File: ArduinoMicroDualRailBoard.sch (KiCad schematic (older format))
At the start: 56 parts, among them J1 Conn_01x20_Male, J10 Conn_01x02_Male, J2 Screw_Terminal_01x03, J3 Conn_01x20_Male, J4 Conn_01x20_Male, J5 Screw_Terminal_01x03, J6 Conn_01x20_Male, J7 SDS-50J, J8 SDS-50J, J9 Screw_Terminal_01x03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

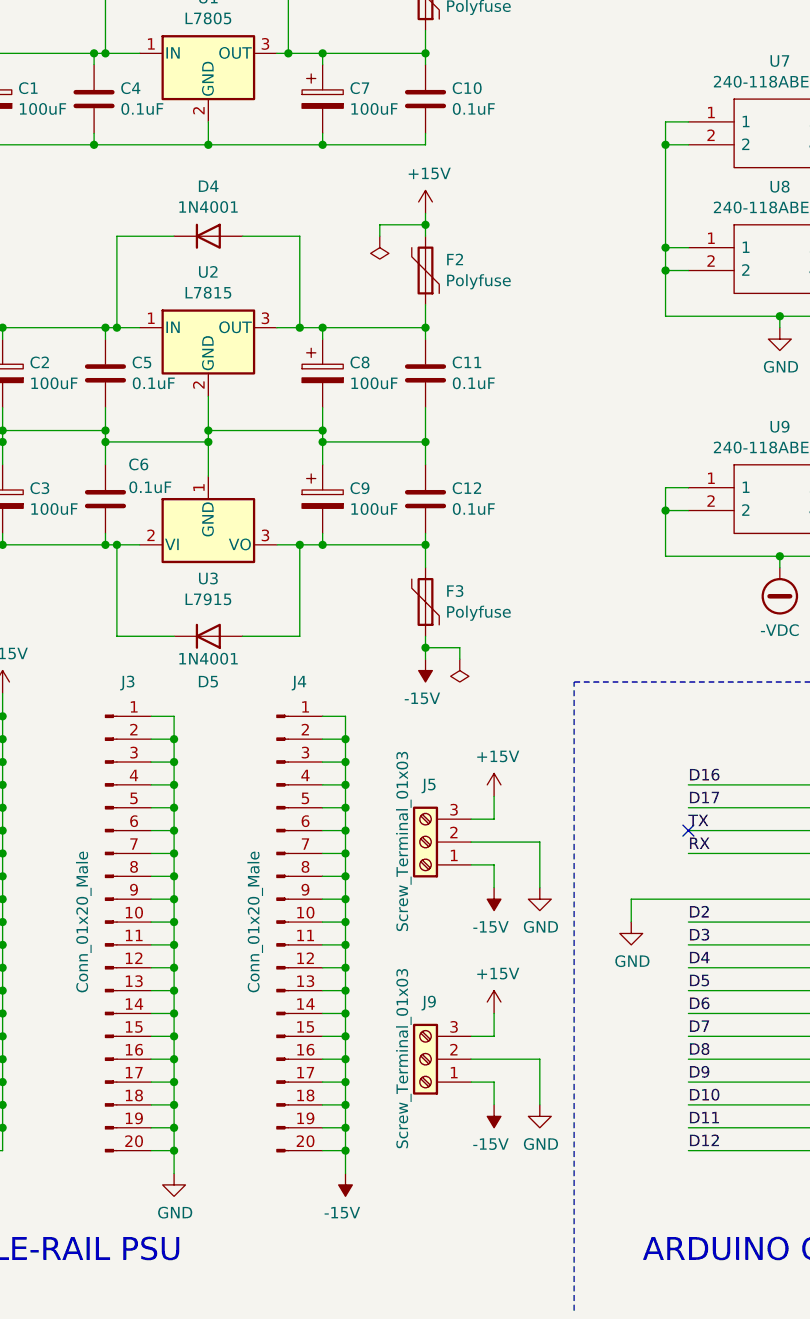
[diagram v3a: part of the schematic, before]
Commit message: Lots of small fixes * Added protection diodes on +/- 15V rails * Fixed 7915 diode direction * Flipped Arduino socket so the USB can actually be plugged in * Added +5V out (since it might be useful to have)
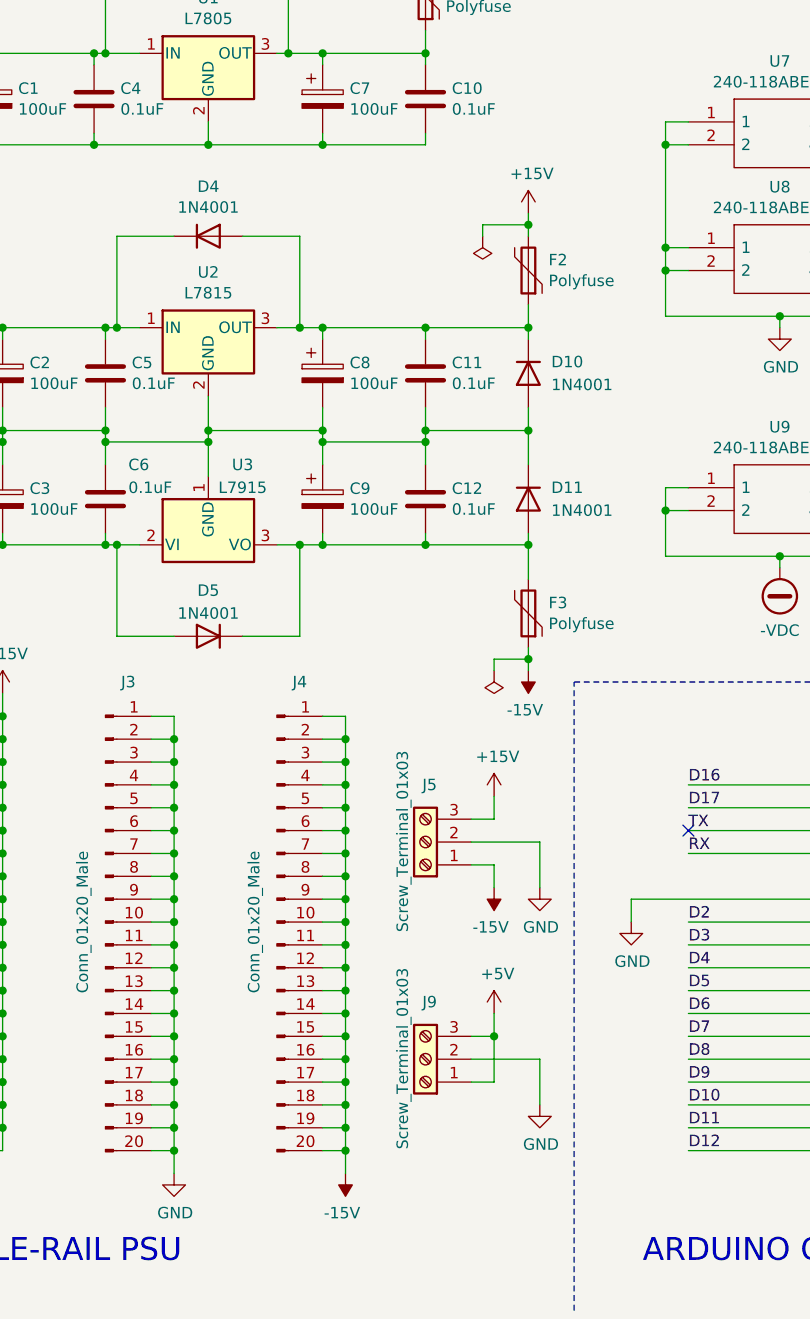
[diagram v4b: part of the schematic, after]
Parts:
- added D10, D11: 1N4001, Diode_THT:D_DO-41_SOD81_P10.16mm_Horizontal, symbol Diode:1N4001
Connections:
- net +15V: no longer J9.3 (Pin_3)
- net +5V: now also J9.1 (Pin_1), J9.3 (Pin_3)
- net -15V: no longer J9.1 (Pin_1)
- net -VDC: now also D5.2 (A); no longer D5.1 (K)
- net GND: now also D10.2 (A), D11.1 (K)
- net at C12.2, C9.2, F3.2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: now also D5.1 (K), D11.2 (A); no longer D5.2 (A)
- net at C11.1, C8.1, D4.2 (A)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: now also D10.1 (K)
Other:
- moved on the sheet: F2, F3
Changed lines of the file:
@@
 L power:+15V #PWR0104
 U 1 1 5FC58BBA
-P 3050 3000
-F 0 "#PWR0104" H 3050 2850 50  0001 C CNN
-F 1 "+15V" H 3065 3173 50  0000 C CNN
-F 2 "" H 3050 3000 50  0001 C CNN
-F 3 "" H 3050 3000 50  0001 C CNN
-	1    3050 3000
+P 3500 3000
+F 0 "#PWR0104" H 3500 2850 50  0001 C CNN
+F 1 "+15V" H 3515 3173 50  0000 C CNN
+F 2 "" H 3500 3000 50  0001 C CNN
+F 3 "" H 3500 3000 50  0001 C CNN
+	1    3500 3000
 	1    0    0    -1
 $EndComp
@@
 	3050 3500 3050 3550
 Wire Wire Line
-	3050 4000 3050 3850
+	3050 4000 3050 3950
 $Comp
 L Connector:Conn_01x20_Male J1
@@
 L power:-15V #PWR0124
 U 1 1 5FC59348
-P 3050 4950
-F 0 "#PWR0124" H 3050 5050 50  0001 C CNN
-F 1 "-15V" H 3065 5123 50  0000 C CNN
-F 2 "" H 3050 4950 50  0001 C CNN
-F 3 "" H 3050 4950 50  0001 C CNN
-	1    3050 4950
+P 3500 5000
+F 0 "#PWR0124" H 3500 5100 50  0001 C CNN
+F 1 "-15V" H 3515 5173 50  0000 C CNN
+F 2 "" H 3500 5000 50  0001 C CNN
+F 3 "" H 3500 5000 50  0001 C CNN
+	1    3500 5000
 	-1   0    0    1
 $EndComp
@@
 F 3 "http://www.vishay.com/docs/88503/1n4001.pdf" H 2100 4850 50  0001 C CNN
 	1    2100 4850
-	1    0    0    1
+	-1   0    0    -1
 $EndComp
 $Comp
@@
 U 1 1 5FBD82BC
 P 2100 4450
-F 0 "U3" H 2100 4301 50  0000 C CNN
-F 1 "L7915" H 2100 4210 50  0000 C CNN
+F 0 "U3" H 2250 4800 50  0000 C CNN
+F 1 "L7915" H 2250 4700 50  0000 C CNN
 F 2 "Package_TO_SOT_THT:TO-220-3_Vertical" H 2100 4250 50  0001 C CIN
 F 3 "http://www.st.com/content/ccc/resource/technical/document/datasheet/c9/16/86/41/c7/2b/45/f2/CD00000450.pdf/files/CD00000450.pdf/jcr:content/translations/en.CD00000450.pdf" H 2100 4450 50  0001 C CNN
@@
 L Device:Polyfuse F3
 U 1 1 5FC1DF2E
-P 3050 4700
-F 0 "F3" H 2962 4654 50  0000 R CNN
-F 1 "Polyfuse" H 2962 4745 50  0000 R CNN
-F 2 "Capacitor_THT:C_Disc_D8.0mm_W2.5mm_P5.00mm" H 3100 4500 50  0001 L CNN
-F 3 "~" H 3050 4700 50  0001 C CNN
-	1    3050 4700
+P 3500 4750
+F 0 "F3" H 3412 4704 50  0000 R CNN
+F 1 "Polyfuse" H 3412 4795 50  0000 R CNN
+F 2 "Capacitor_THT:C_Disc_D8.0mm_W2.5mm_P5.00mm" H 3550 4550 50  0001 L CNN
+F 3 "~" H 3500 4750 50  0001 C CNN
+	1    3500 4750
 	-1   0    0    1
 $EndComp
@@
 L Device:Polyfuse F2
 U 1 1 5FC20AC7
-P 3050 3250
-F 0 "F2" H 2962 3204 50  0000 R CNN
-F 1 "Polyfuse" H 2962 3295 50  0000 R CNN
-F 2 "Capacitor_THT:C_Disc_D8.0mm_W2.5mm_P5.00mm" H 3100 3050 50  0001 L CNN
-F 3 "~" H 3050 3250 50  0001 C CNN
-	1    3050 3250
+P 3500 3250
+F 0 "F2" H 3412 3204 50  0000 R CNN
+F 1 "Polyfuse" H 3412 3295 50  0000 R CNN
+F 2 "Capacitor_THT:C_Disc_D8.0mm_W2.5mm_P5.00mm" H 3550 3050 50  0001 L CNN
+F 3 "~" H 3500 3250 50  0001 C CNN
+	1    3500 3250
 	-1   0    0    1
 $EndComp
 Wire Wire Line
-	3050 4850 3050 4900
-Wire Wire Line
-	3050 4450 3050 4550
-Connection ~ 3050 4450
-Wire Wire Line
-	3050 3400 3050 3500
+	3500 4900 3500 4950
+Wire Wire Line
+	3500 3400 3500 3500
 Connection ~ 3050 3500
 Wire Wire Line
-	3050 3000 3050 3050
+	3500 3000 3500 3050
 Wire Wire Line
 	3050 1800 3050 1850
@@
 L power:PWR_FLAG #FLG0103
 U 1 1 5FC109BA
-P 3200 4950
-F 0 "#FLG0103" H 3200 5025 50  0001 C CNN
-F 1 "PWR_FLAG" H 3200 5123 50  0001 C CNN
-F 2 "" H 3200 4950 50  0001 C CNN
-F 3 "~" H 3200 4950 50  0001 C CNN
-	1    3200 4950
+P 3350 5000
+F 0 "#FLG0103" H 3350 5075 50  0001 C CNN
+F 1 "PWR_FLAG" H 3350 5173 50  0001 C CNN
+F 2 "" H 3350 5000 50  0001 C CNN
+F 3 "~" H 3350 5000 50  0001 C CNN
+	1    3350 5000
 	-1   0    0    1
 $EndComp
 Wire Wire Line
-	3200 4900 3200 4950
-Wire Wire Line
-	3050 4900 3200 4900
-Connection ~ 3050 4900
-Wire Wire Line
-	3050 4900 3050 4950
+	3350 4950 3350 5000
+Wire Wire Line
+	3500 4950 3350 4950
+Connection ~ 3500 4950
+Wire Wire Line
+	3500 4950 3500 5000
 $Comp
 L power:PWR_FLAG #FLG0105
 U 1 1 5FC672D3
-P 2850 3100
-F 0 "#FLG0105" H 2850 3175 50  0001 C CNN
-F 1 "PWR_FLAG" H 2850 3273 50  0001 C CNN
-F 2 "" H 2850 3100 50  0001 C CNN
-F 3 "~" H 2850 3100 50  0001 C CNN
-	1    2850 3100
+P 3300 3100
+F 0 "#FLG0105" H 3300 3175 50  0001 C CNN
+F 1 "PWR_FLAG" H 3300 3273 50  0001 C CNN
+F 2 "" H 3300 3100 50  0001 C CNN
+F 3 "~" H 3300 3100 50  0001 C CNN
+	1    3300 3100
 	-1   0    0    1
 $EndComp
 Wire Wire Line
-	3050 3050 2850 3050
-Wire Wire Line
-	2850 3050 2850 3100
-Connection ~ 3050 3050
-Wire Wire Line
-	3050 3050 3050 3100
+	3500 3050 3300 3050
+Wire Wire Line
+	3300 3050 3300 3100
+Connection ~ 3500 3050
+Wire Wire Line
+	3500 3050 3500 3100
 Wire Wire Line
 	3050 1850 2850 1850
@@
 $EndComp
 $Comp
-L power:+15V #PWR01
-U 1 1 5FC225E1
-P 3350 6500
-F 0 "#PWR01" H 3350 6350 50  0001 C CNN
-F 1 "+15V" H 3365 6673 50  0000 C CNN
-F 2 "" H 3350 6500 50  0001 C CNN
-F 3 "" H 3350 6500 50  0001 C CNN
-	1    3350 6500
-	1    0    0    -1
-$EndComp
-$Comp
 L power:GND #PWR03
 U 1 1 5FC225E7
@@
 	1    0    0    -1
 $EndComp
-$Comp
-L power:-15V #PWR02
-U 1 1 5FC225ED
-P 3350 6900
-F 0 "#PWR02" H 3350 7000 50  0001 C CNN
-F 1 "-15V" H 3365 7073 50  0000 C CNN
-F 2 "" H 3350 6900 50  0001 C CNN
-F 3 "" H 3350 6900 50  0001 C CNN
-	1    3350 6900
-	-1   0    0    1
-$EndComp
 Wire Wire Line
 	3250 6800 3350 6800
-Wire Wire Line
-	3350 6800 3350 6900
 Wire Wire Line
 	3250 6700 3550 6700
@@
 Wire Wire Line
 	6400 6000 6500 6000
+$Comp
+L power:+5V #PWR0136
+U 1 1 5FC69BAF
+P 3350 6500
+F 0 "#PWR0136" H 3350 6350 50  0001 C CNN
+F 1 "+5V" H 3365 6673 50  0000 C CNN
+F 2 "" H 3350 6500 50  0001 C CNN
+F 3 "" H 3350 6500 50  0001 C CNN
+	1    3350 6500
+	1    0    0    -1
+$EndComp
+Wire Wire Line
+	3350 6800 3350 6600
+Connection ~ 3350 6600
+$Comp
+L Diode:1N4001 D11
+U 1 1 5FD3EB32
+P 3500 4250
+F 0 "D11" V 3450 4150 50  0000 R CNN
+F 1 "1N4001" V 3550 4150 50  0000 R CNN
+F 2 "Diode_THT:D_DO-41_SOD81_P10.16mm_Horizontal" H 3500 4075 50  0001 C CNN
+F 3 "http://www.vishay.com/docs/88503/1n4001.pdf" H 3500 4250 50  0001 C CNN
+	1    3500 4250
+	0    -1   1    0
+$EndComp
+$Comp
+L Diode:1N4001 D10
+U 1 1 5FD3FB5B
+P 3500 3700
+F 0 "D10" V 3450 3600 50  0000 R CNN
+F 1 "1N4001" V 3550 3600 50  0000 R CNN
+F 2 "Diode_THT:D_DO-41_SOD81_P10.16mm_Horizontal" H 3500 3525 50  0001 C CNN
+F 3 "http://www.vishay.com/docs/88503/1n4001.pdf" H 3500 3700 50  0001 C CNN
+	1    3500 3700
+	0    -1   1    0
+$EndComp
+Wire Wire Line
+	3500 4400 3500 4450
+Wire Wire Line
+	3500 4450 3050 4450
+Connection ~ 3500 4450
+Wire Wire Line
+	3500 4450 3500 4600
+Connection ~ 3050 4450
+Wire Wire Line
+	3050 3950 3500 3950
+Wire Wire Line
+	3500 3950 3500 3850
+Connection ~ 3050 3950
+Wire Wire Line
+	3050 3950 3050 3850
+Wire Wire Line
+	3500 3950 3500 4100
+Connection ~ 3500 3950
+Wire Wire Line
+	3050 3500 3500 3500
+Wire Wire Line
+	3500 3500 3500 3550
+Connection ~ 3500 3500
 $EndSCHEMATC

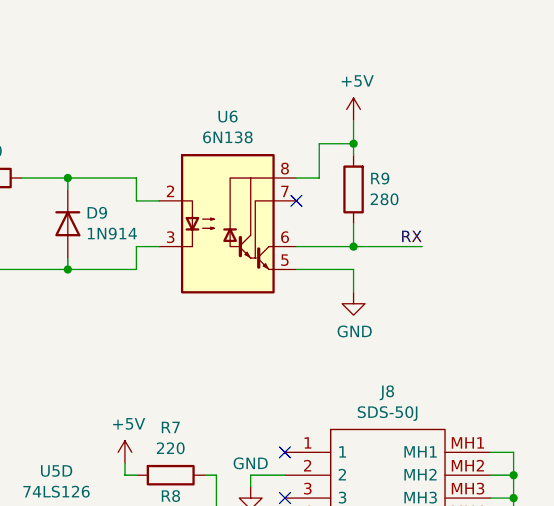
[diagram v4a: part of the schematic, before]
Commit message: Added bypass cap for 6N138
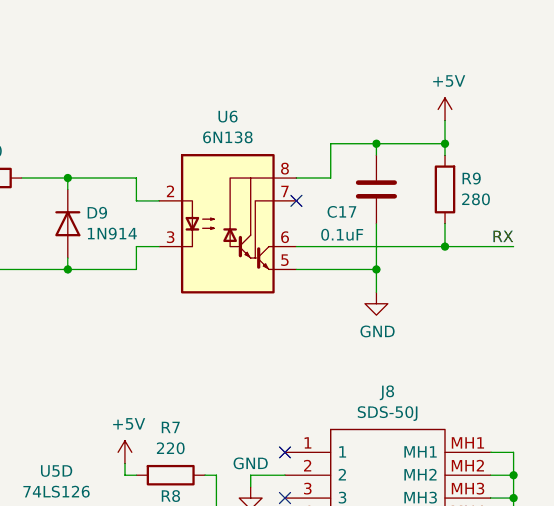
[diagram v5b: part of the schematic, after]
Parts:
- added C17: 0.1uF, Capacitor_THT:C_Disc_D4.3mm_W1.9mm_P5.00mm, symbol Device:C
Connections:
- net +5V: now also C17.2
- net GND: now also C17.1
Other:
- moved on the sheet: R9
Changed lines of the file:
@@
 L Device:R R9
 U 1 1 60052C2E
-P 10150 1250
-F 0 "R9" H 10080 1204 50  0000 R CNN
-F 1 "280" H 10080 1295 50  0000 R CNN
-F 2 "Resistor_THT:R_Axial_DIN0204_L3.6mm_D1.6mm_P5.08mm_Horizontal" V 10080 1250 50  0001 C CNN
-F 3 "~" H 10150 1250 50  0001 C CNN
-	1    10150 1250
+P 10550 1250
+F 0 "R9" H 10480 1204 50  0000 R CNN
+F 1 "280" H 10480 1295 50  0000 R CNN
+F 2 "Resistor_THT:R_Axial_DIN0204_L3.6mm_D1.6mm_P5.08mm_Horizontal" V 10480 1250 50  0001 C CNN
+F 3 "~" H 10550 1250 50  0001 C CNN
+	1    10550 1250
 	-1   0    0    1
 $EndComp
@@
 L power:GND #PWR0117
 U 1 1 6005A2B8
-P 10150 1700
-F 0 "#PWR0117" H 10150 1450 50  0001 C CNN
-F 1 "GND" H 10155 1527 50  0000 C CNN
-F 2 "" H 10150 1700 50  0001 C CNN
-F 3 "" H 10150 1700 50  0001 C CNN
-	1    10150 1700
+P 10250 1700
+F 0 "#PWR0117" H 10250 1450 50  0001 C CNN
+F 1 "GND" H 10255 1527 50  0000 C CNN
+F 2 "" H 10250 1700 50  0001 C CNN
+F 3 "" H 10250 1700 50  0001 C CNN
+	1    10250 1700
 	1    0    0    -1
 $EndComp
@@
 L power:+5V #PWR0118
 U 1 1 6005BB0B
-P 10150 950
-F 0 "#PWR0118" H 10150 800 50  0001 C CNN
-F 1 "+5V" H 10165 1123 50  0000 C CNN
-F 2 "" H 10150 950 50  0001 C CNN
-F 3 "" H 10150 950 50  0001 C CNN
-	1    10150 950
+P 10550 950
+F 0 "#PWR0118" H 10550 800 50  0001 C CNN
+F 1 "+5V" H 10565 1123 50  0000 C CNN
+F 2 "" H 10550 950 50  0001 C CNN
+F 3 "" H 10550 950 50  0001 C CNN
+	1    10550 950
 	1    0    0    -1
 $EndComp
@@
 	8900 1600 7650 1600
 Wire Wire Line
-	9900 1200 10000 1200
-Wire Wire Line
-	10000 1200 10000 1050
-Wire Wire Line
-	10000 1050 10150 1050
-Wire Wire Line
-	10150 1050 10150 1100
-Wire Wire Line
-	10150 950  10150 1050
-Connection ~ 10150 1050
-Wire Wire Line
-	9900 1500 10150 1500
-Wire Wire Line
-	10150 1500 10150 1400
-Wire Wire Line
-	10150 1500 10450 1500
-Connection ~ 10150 1500
-Wire Wire Line
-	10150 1600 10150 1700
-Wire Wire Line
-	9900 1600 10150 1600
-Text Label 10450 1500 2    50   ~ 0
+	10550 1050 10550 1100
+Wire Wire Line
+	10550 950  10550 1050
+Connection ~ 10550 1050
+Wire Wire Line
+	10550 1500 10550 1400
+Wire Wire Line
+	10550 1500 10850 1500
+Connection ~ 10550 1500
+Wire Wire Line
+	10250 1600 10250 1700
+Wire Wire Line
+	9900 1600 10250 1600
+Text Label 10850 1500 2    50   ~ 0
 RX
 $Comp
@@
 	3500 3500 3500 3550
 Connection ~ 3500 3500
+$Comp
+L Device:C C17
+U 1 1 5FC90C85
+P 10250 1250
+F 0 "C17" H 10400 1350 50  0000 C CNN
+F 1 "0.1uF" H 10400 1450 50  0000 C CNN
+F 2 "Capacitor_THT:C_Disc_D4.3mm_W1.9mm_P5.00mm" H 10288 1100 50  0001 C CNN
+F 3 "~" H 10250 1250 50  0001 C CNN
+	1    10250 1250
+	-1   0    0    1
+$EndComp
+Wire Wire Line
+	10050 1050 10050 1200
+Wire Wire Line
+	10050 1200 9900 1200
+Wire Wire Line
+	10050 1050 10250 1050
+Wire Wire Line
+	10250 1050 10250 1100
+Connection ~ 10250 1050
+Wire Wire Line
+	10250 1050 10550 1050
+Wire Wire Line
+	9900 1500 10550 1500
+Wire Wire Line
+	10250 1600 10250 1400
+Connection ~ 10250 1600
 $EndSCHEMATC

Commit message: Regenerated gerbers, minor rerouting
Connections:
- net +15V: now also J5.1 (Pin_1); no longer J5.3 (Pin_3)
- net -15V: now also J5.3 (Pin_3); no longer J5.1 (Pin_1)
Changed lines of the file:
@@
 F 3 "~" H 3050 5750 50  0001 C CNN
 	1    3050 5750
-	-1   0    0    1
+	-1   0    0    -1
 $EndComp
 $Comp
